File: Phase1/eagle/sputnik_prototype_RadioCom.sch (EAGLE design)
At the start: 56 parts, among them Y1 32MHz

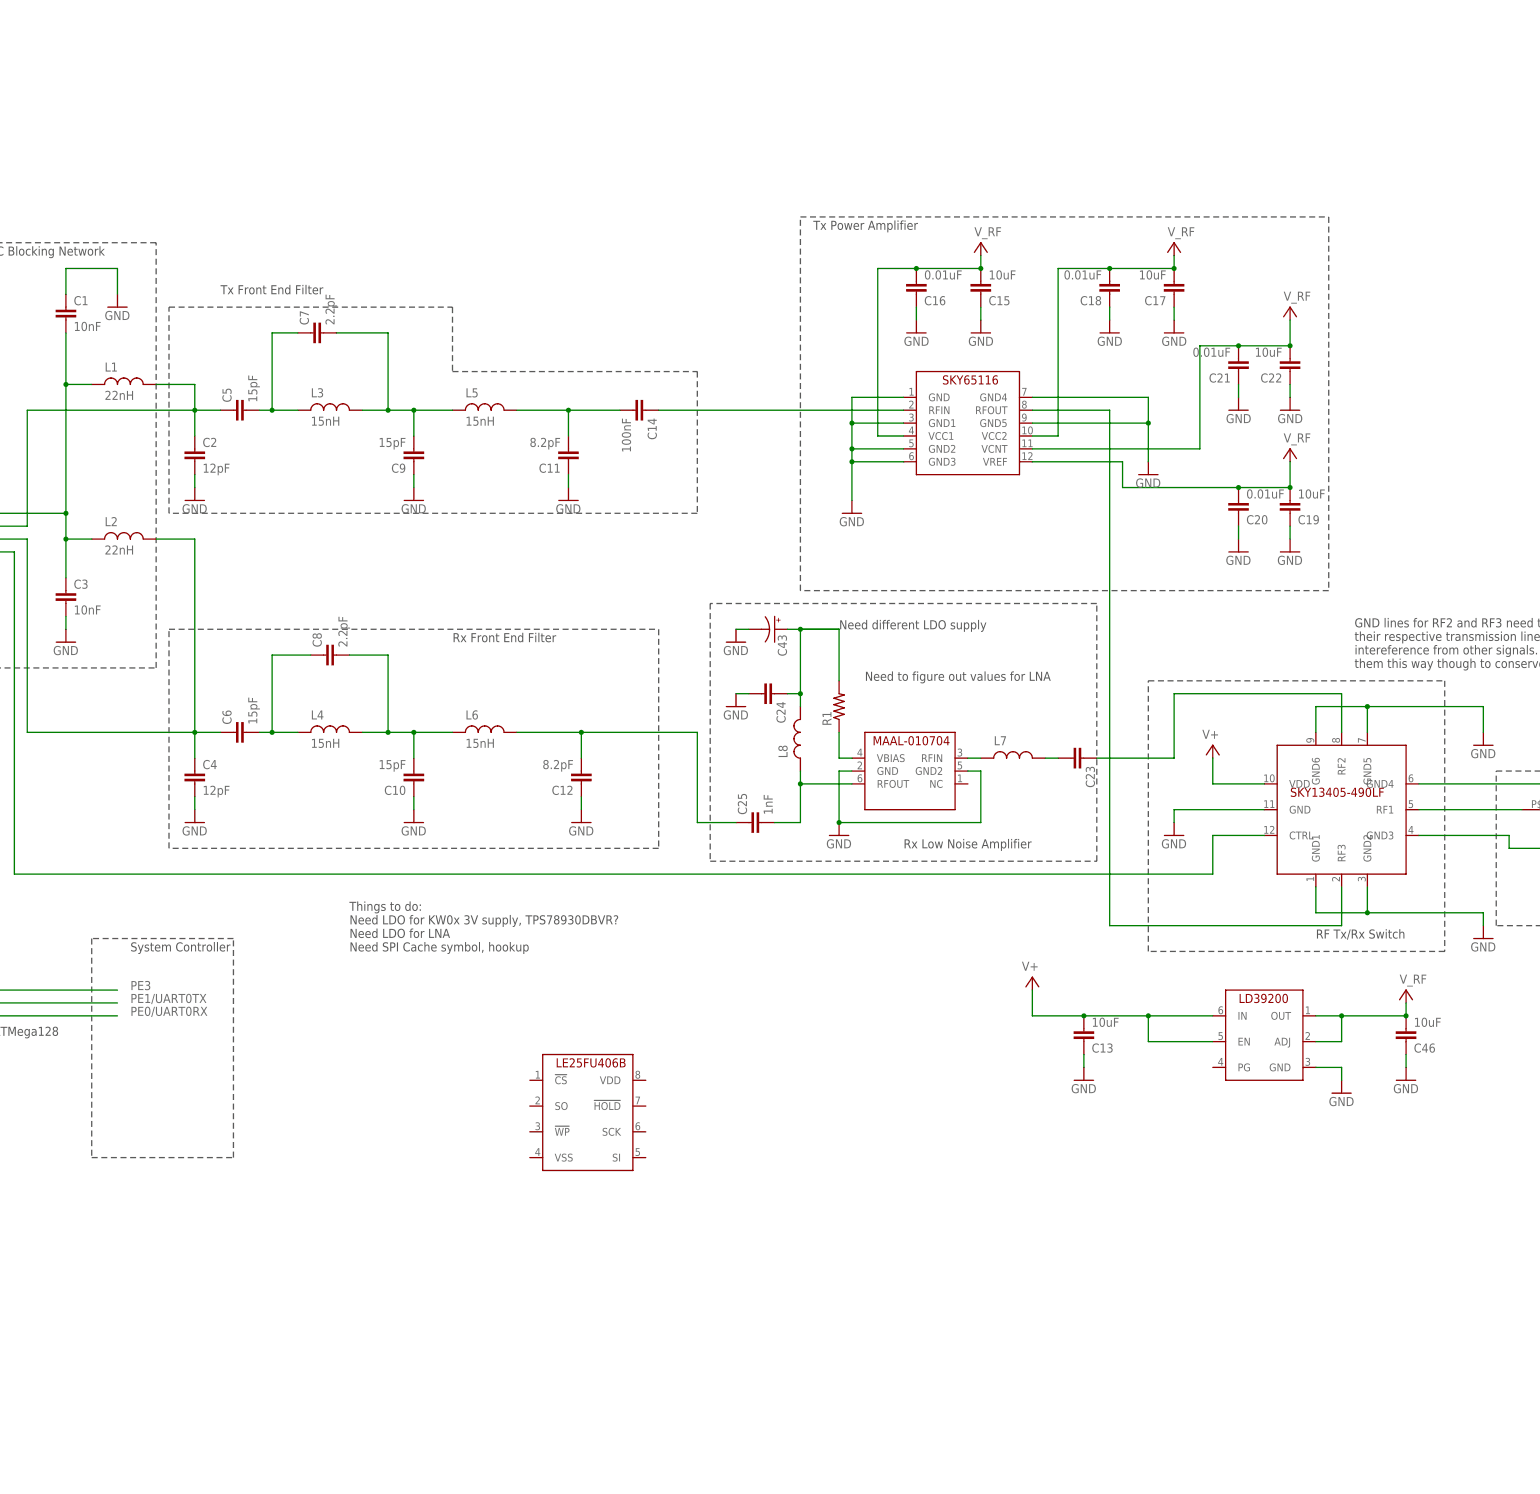
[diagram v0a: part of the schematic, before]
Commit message: Added LNA LDO footprint and circuitry
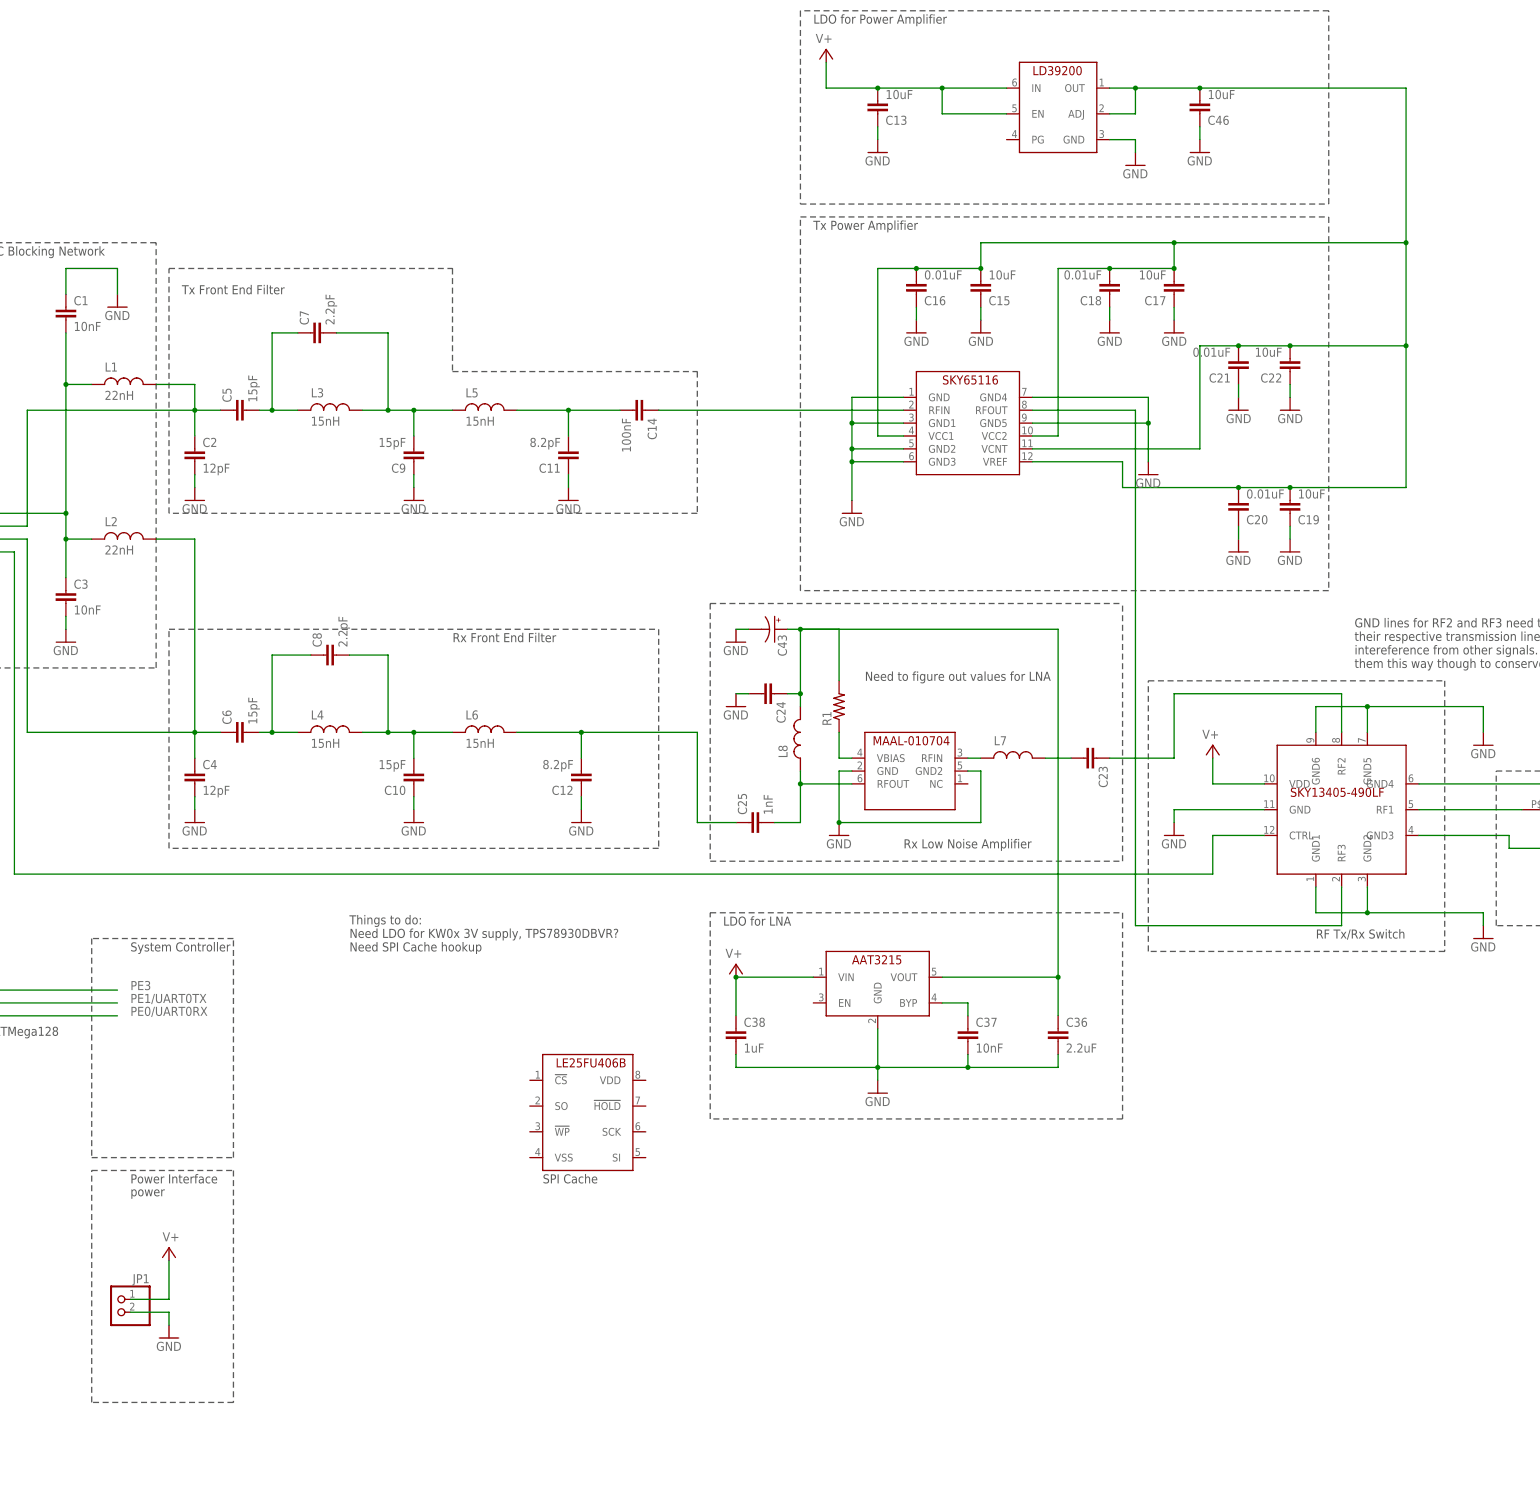
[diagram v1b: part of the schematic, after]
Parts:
- added C36: 2.2uF, rcl_custom:C-EU0402-B-NOSILK
- added C37: 10nF, rcl_custom:C-EU0402-B-NOSILK
- added C38: 1uF, rcl_custom:C-EU0402-B-NOSILK
- added JP1: (no value), psas_c3_team05:PINHD-1X2
- added U$7: AAT3215, psas_c3_team05:AAT3215
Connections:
- new net N$1: C37.1, U$7.BYP
- new net N$9: C36.1, U$7.VOUT
- new net VPA: C15.2, C16.2, C17.2, C18.2, C19.2, C20.2, C21.2, C22.2, C46.2, U$6.VCC1, U$6.VCC2, U$6.VCNT, U$6.VREF, U$9.ADJ, U$9.OUT
- net GND: now also C36.2, C37.2, C38.2, JP1.2, U$7.GND
- net V+: now also C38.1, JP1.1, U$7.VIN; no longer C15.2, C16.2, C17.2, C18.2, C19.2, C20.2, C21.2, C22.2, C46.2, U$6.VCC1, U$6.VCC2, U$6.VCNT, U$6.VREF, U$9.ADJ, U$9.OUT
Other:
- note added: "LDO for LNA"
- note added: "LDO for Power Amplifier"
- note added: "Power Interface"
- note added: "SPI Cache"
- note added: "Things to do: Need LDO for KW0x 3V supply, TPS78930DBVR? Need SPI Cache hookup"
- note added: "power"
- note removed: "Need different LDO supply"
- note removed: "Things to do: Need LDO for KW0x 3V supply, TPS78930DBVR? Need LDO for LNA Need SPI Cache symbol, hookup"
- moved on the sheet: C13, C23, C46

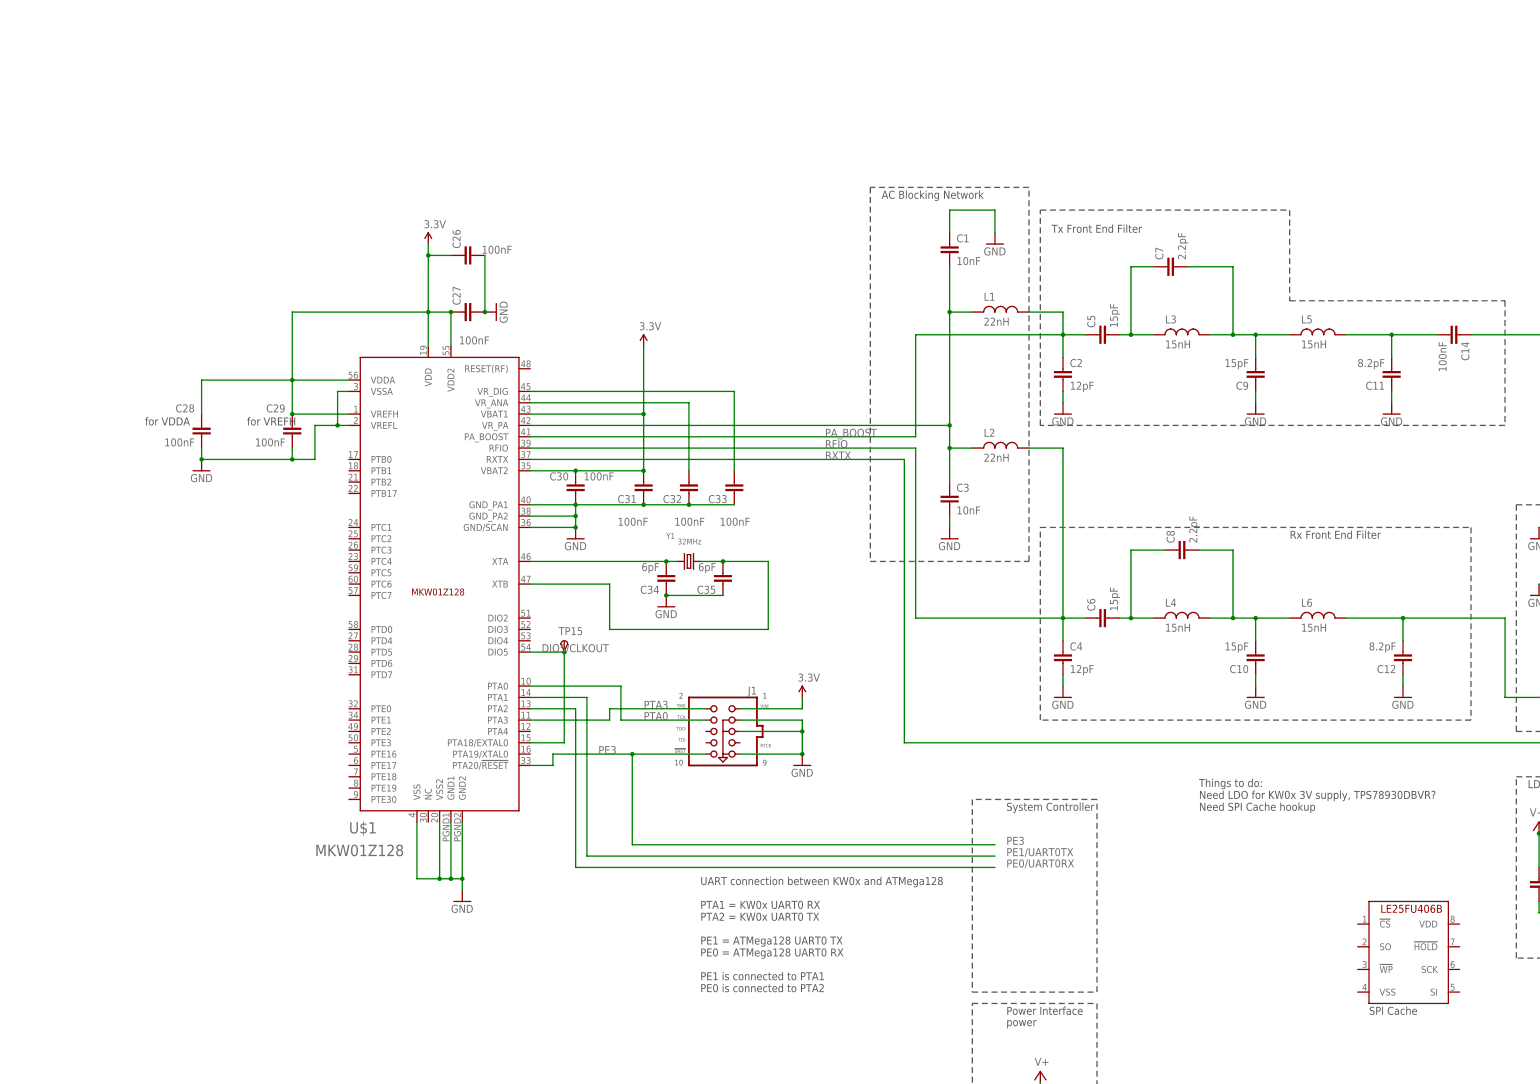
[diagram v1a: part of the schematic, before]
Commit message: Added LDO for KW0x
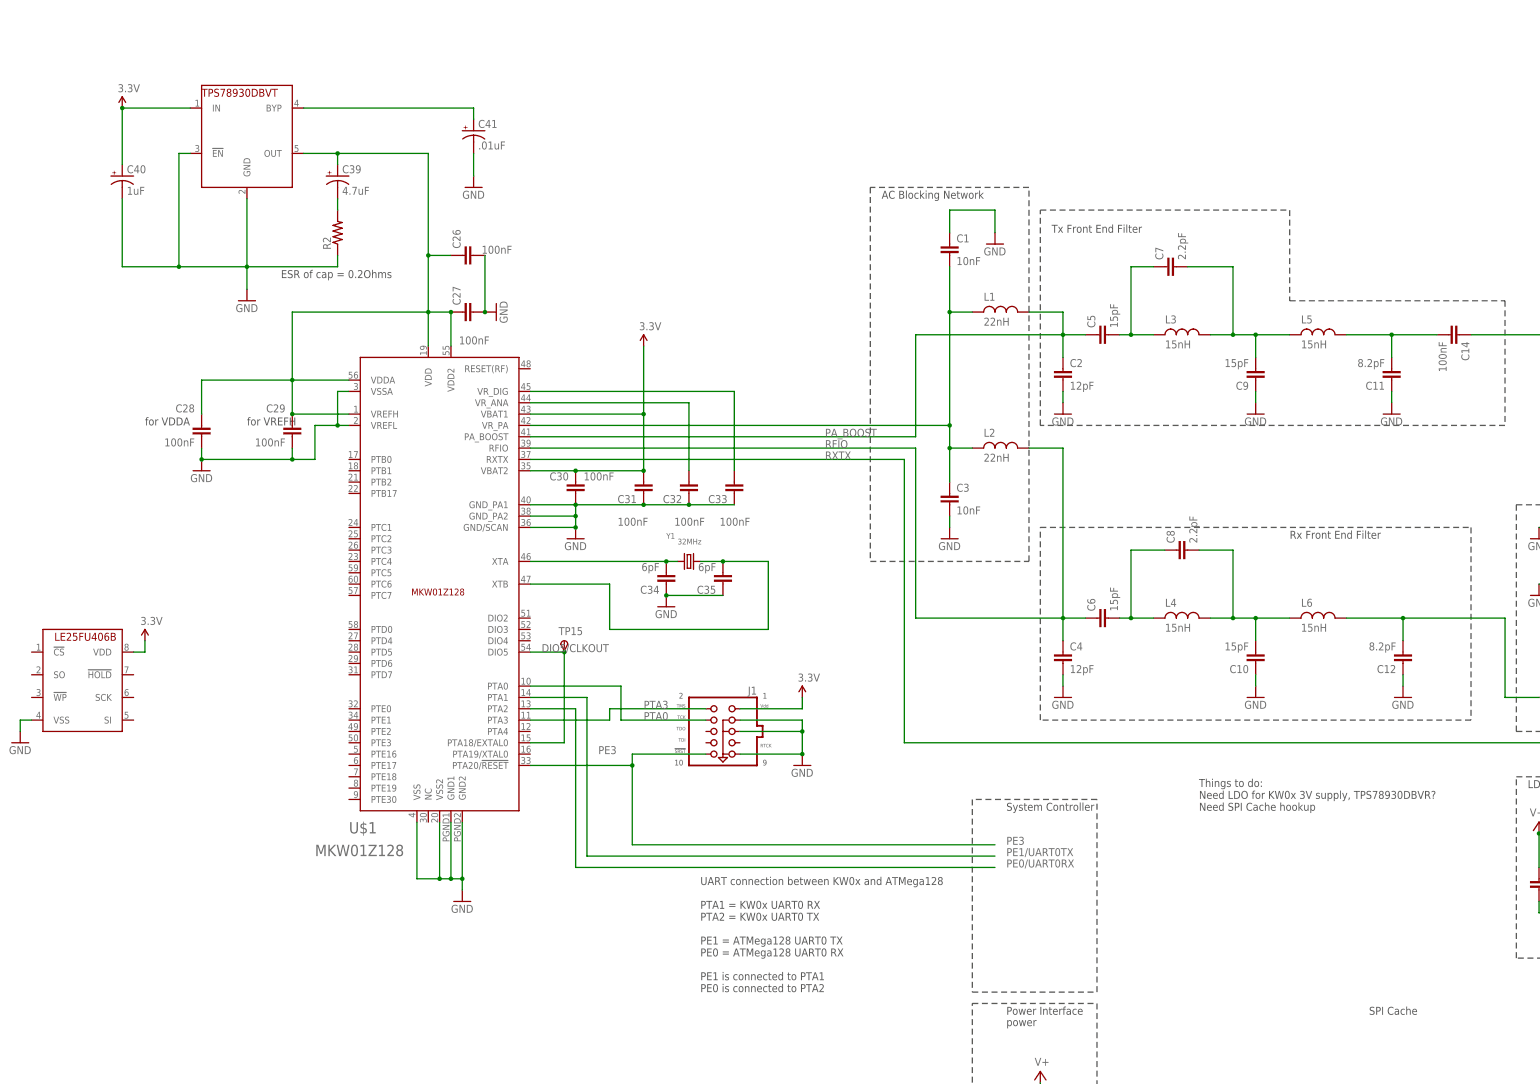
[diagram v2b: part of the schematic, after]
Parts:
- added C39: 4.7uF, rcl:CPOL-USCT6032
- added C40: 1uF, rcl:CPOL-USCT6032
- added C41: .01uF, rcl:CPOL-USCT6032
- added R2: (no value), rcl_custom:R-US_0603-B-NOSILK
- added U$8: TPS78930DBVT, psas_c3_team05:TPS78930DBVT
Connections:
- new net N$11: C41.+, U$8.BYP
- new net N$13: C39.-, R2.2
- new net N$3: C26.1, C27.1, C28.2, C29.2, C39.+, U$1.VDD, U$1.VDD2, U$1.VDDA, U$1.VREFH, U$8.OUT
- net 3.3V: now also C40.+, U$3.VDD, U$8.IN; no longer C26.1, C27.1, C28.2, C29.2, U$1.VDD, U$1.VDD2, U$1.VDDA, U$1.VREFH
- net GND: now also C40.-, C41.-, R2.1, U$3.VSS, U$8.!EN, U$8.GND
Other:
- note added: "ESR of cap = 0.2Ohms"

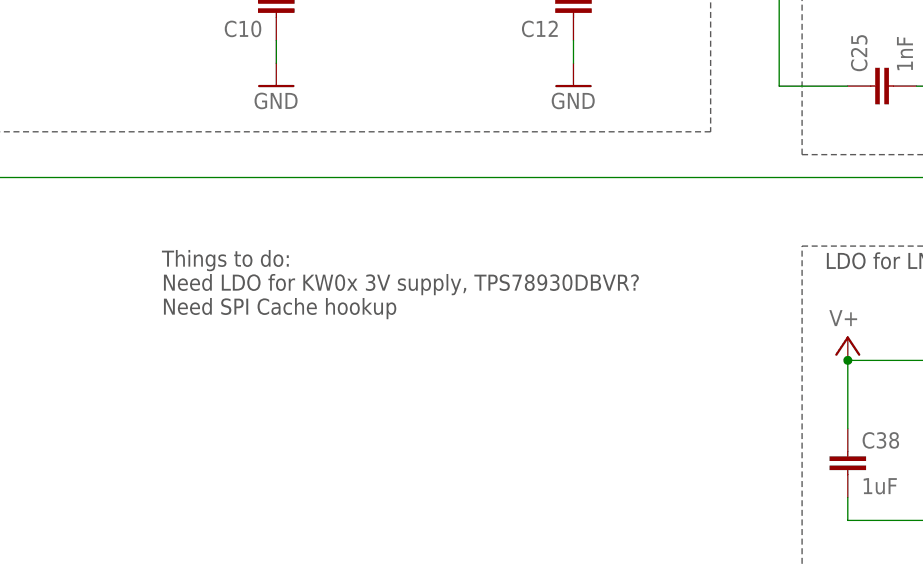
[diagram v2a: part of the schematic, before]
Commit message: Updated to do lists
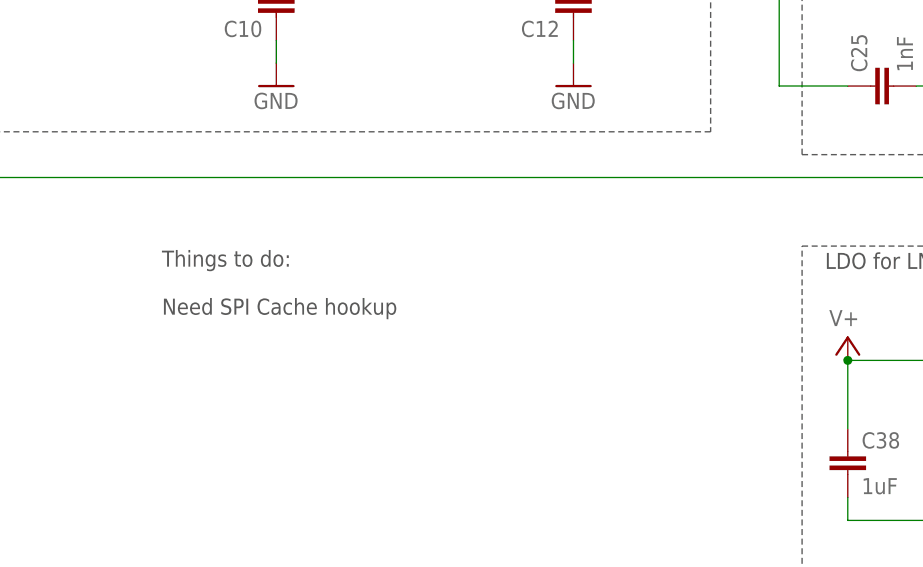
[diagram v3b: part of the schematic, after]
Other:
- note added: "Things to do: Need SPI Cache hookup"
- note removed: "Things to do: Need LDO for KW0x 3V supply, TPS78930DBVR? Need SPI Cache hookup"
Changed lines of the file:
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@@
 <text x="241.3" y="147.32" size="1.778" layer="97">System Controller</text>
 <text x="284.48" y="147.32" size="1.778" layer="97">Things to do:
-Need LDO for KW0x 3V supply, TPS78930DBVR?
 Need SPI Cache hookup</text>
 <text x="322.58" y="101.6" size="1.778" layer="97">SPI Cache</text>
